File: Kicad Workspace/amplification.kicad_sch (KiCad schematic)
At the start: 1 part, among them U5 TPA3255DDV

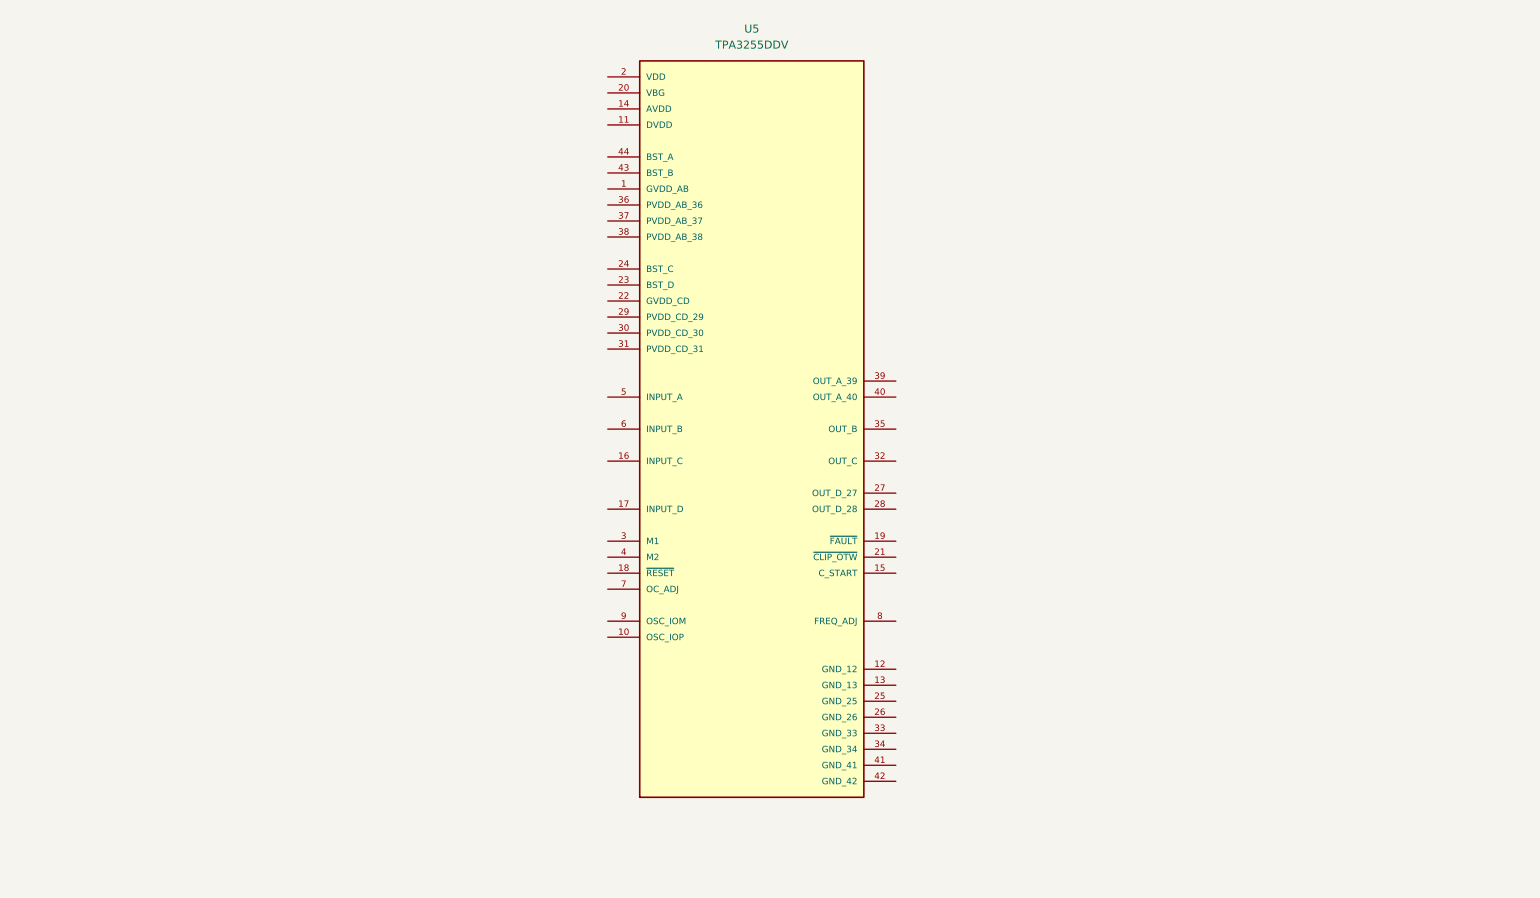
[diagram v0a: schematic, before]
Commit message: feat: ampli stage work in progress
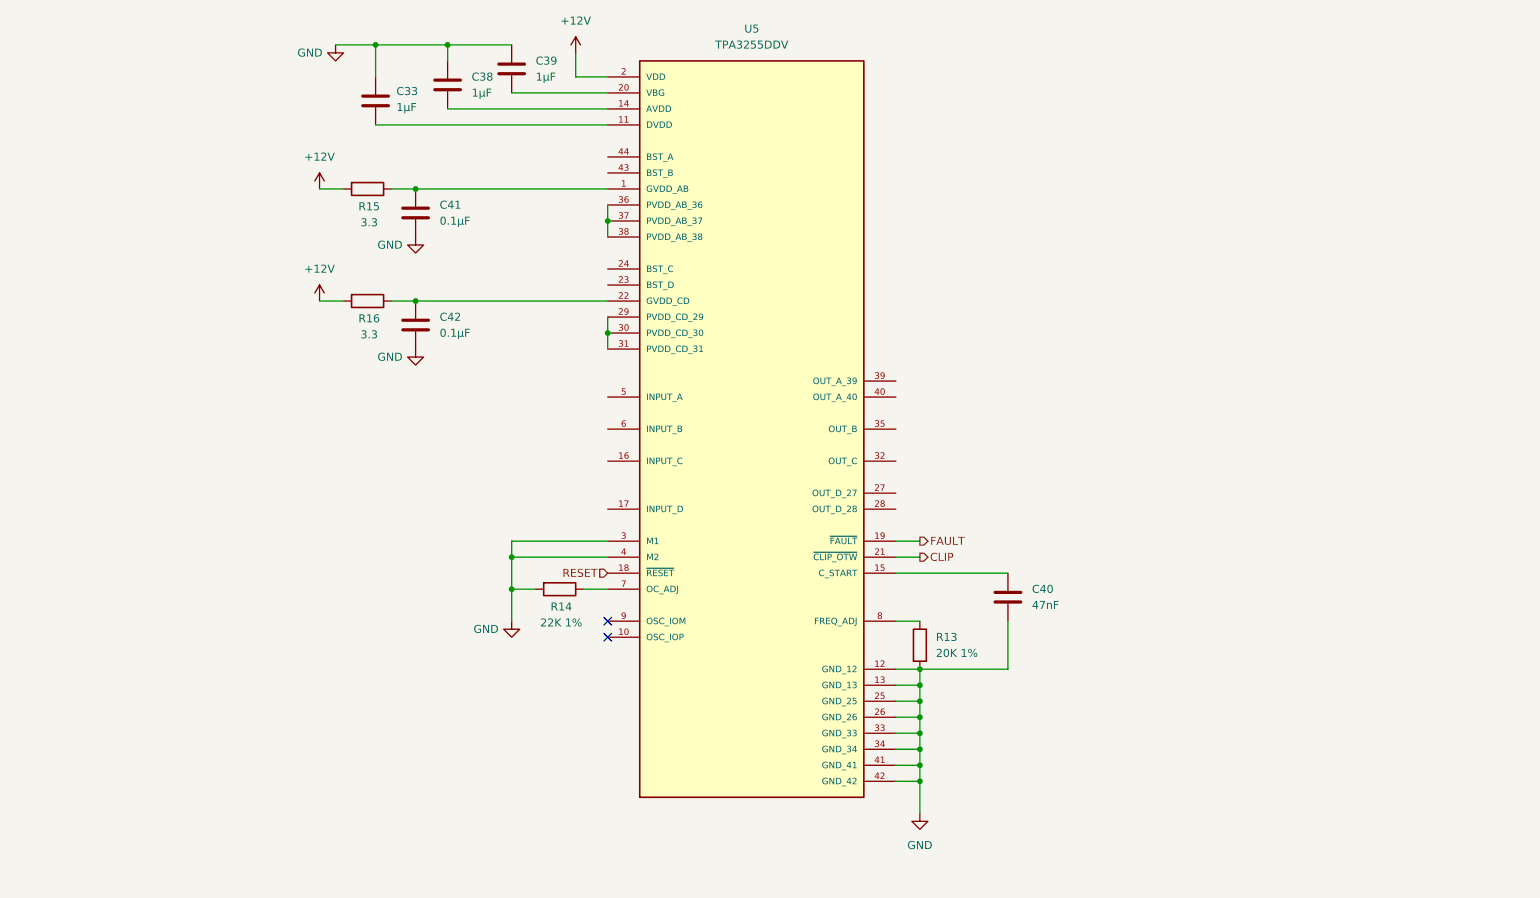
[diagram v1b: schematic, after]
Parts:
- added C33, C38, C39: 1µF, Capacitor_SMD:C_0201_0603Metric, symbol Device:C
- added C40: 47nF, Capacitor_SMD:C_0201_0603Metric, symbol Device:C
- added C41, C42: 0.1µF, Capacitor_SMD:C_01005_0402Metric, symbol Device:C
- added R13: 20K 1%, Resistor_SMD:R_0805_2012Metric, symbol Device:R
- added R14: 22K 1%, Resistor_SMD:R_0805_2012Metric, symbol Device:R
- added R15, R16: 3.3, Resistor_SMD:R_0201_0603Metric, symbol Device:R
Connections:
- net at U5.1 (GVDD_AB): now also C41.2, R15.1
- net at U5.11 (DVDD): now also C33.2
- net GND: now reaches U5.12 (GND_12)
- net GND: now also U5.13 (GND_13), U5.25 (GND_25), U5.26 (GND_26), U5.3 (M1), U5.33 (GND_33), U5.34 (GND_34), U5.4 (M2), U5.41 (GND_41), U5.42 (GND_42), C33.1, C38.2, C39.2, C40.2, C41.1, C42.1, R13.2, R14.2
- net at U5.14 (AVDD): now also C38.1
- net at U5.15 (C_START): now also C40.1
- net RESET: now reaches U5.18 (~{RESET})
- net FAULT: now reaches U5.19 (~{FAULT})
- net +12V: now reaches U5.2 (VDD)
- net +12V: now also R15.2, R16.2
- net at U5.20 (VBG): now also C39.1
- net CLIP: now reaches U5.21 (~{CLIP_OTW})
- net at U5.22 (GVDD_CD): now also C42.2, R16.1
- net at U5.29 (PVDD_CD_29): now also U5.30 (PVDD_CD_30), U5.31 (PVDD_CD_31)
- net at U5.36 (PVDD_AB_36): now also U5.37 (PVDD_AB_37), U5.38 (PVDD_AB_38)
- net at U5.7 (OC_ADJ): now also R14.1
- net at U5.8 (FREQ_ADJ): now also R13.1
- no-connect marks 0 -> 2

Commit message: feat: TPA3255 power 48V + clean output
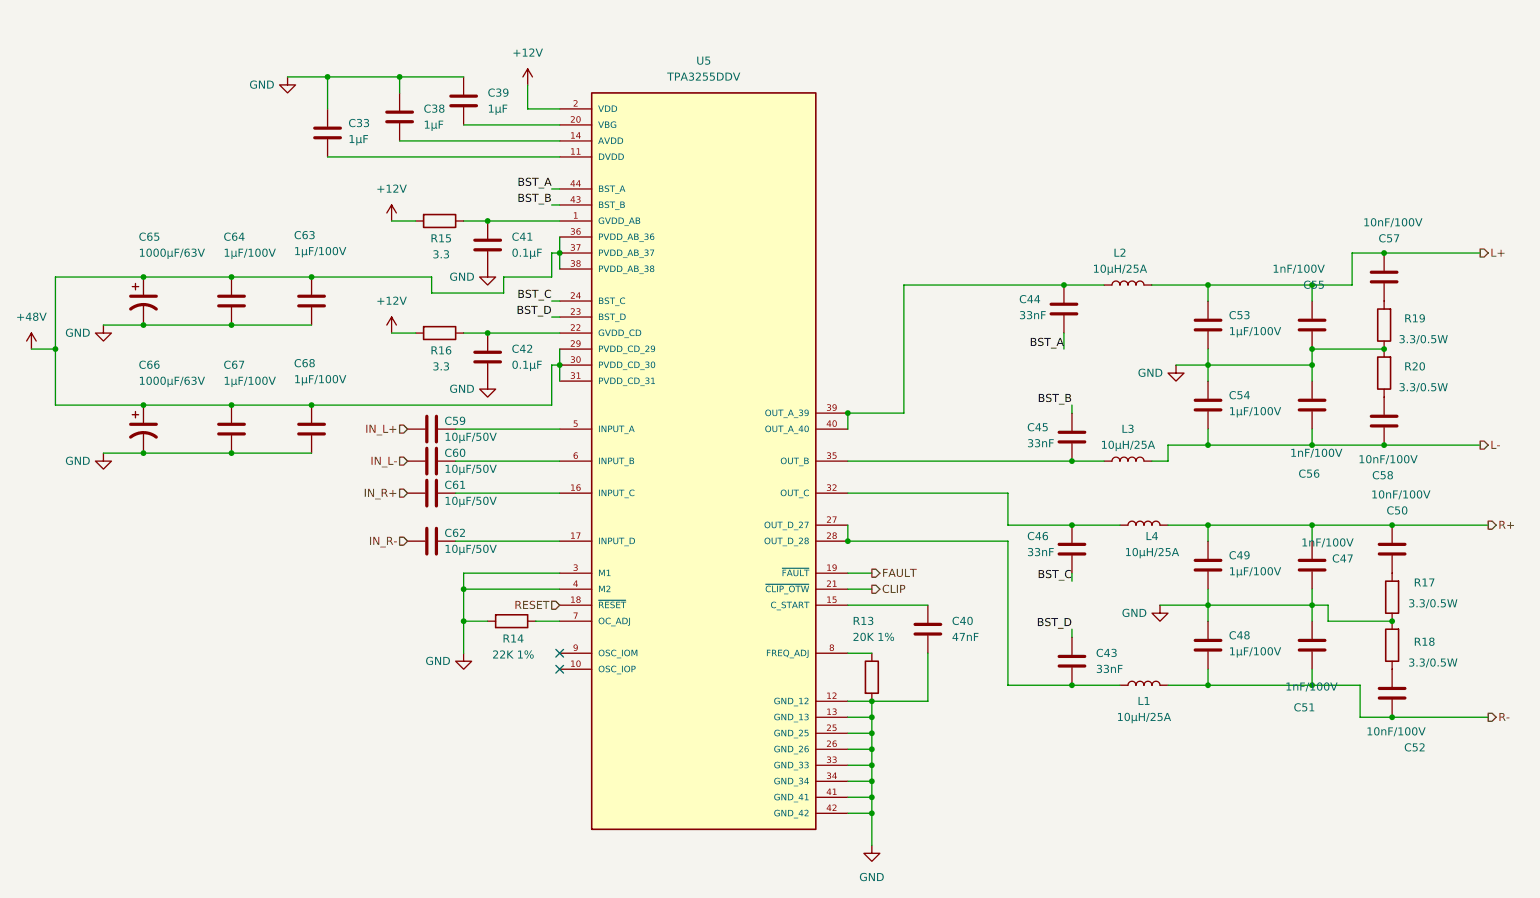
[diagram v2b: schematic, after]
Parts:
- added C43, C44, C45, C46: 33nF, Capacitor_SMD:C_0201_0603Metric, symbol Device:C
- added C47, C51, C55, C56: 1nF/100V, Capacitor_SMD:C_0201_0603Metric, symbol Device:C
- added C48, C49, C53, C54, C63, C64, C67, C68: 1µF/100V, Capacitor_THT:C_Rect_L10.0mm_W4.0mm_P7.50mm_MKS4, symbol Device:C
- added C50, C52, C57, C58: 10nF/100V, Capacitor_SMD:C_0805_2012Metric, symbol Device:C
- added C59, C60, C61, C62: 10µF/50V, Capacitor_THT:C_Radial_D6.3mm_H11.0mm_P2.50mm, symbol Device:C
- added C65, C66: 1000µF/63V, Capacitor_THT:CP_Radial_D16.0mm_P7.50mm, symbol Device:C_Polarized_US
- added L1, L2, L3, L4: 10µH/25A, symbol Device:L
- added R17, R18, R19, R20: 3.3/0.5W, Resistor_SMD:R_1206_3216Metric, symbol Device:R
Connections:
- net GND: now also C47.1, C48.1, C49.2, C51.2, C53.2, C54.1, C55.1, C56.2, C63.2, C64.2, C65.2, C66.2, C67.2, C68.2, R17.1, R18.2, R19.1, R20.2
- net at U5.16 (INPUT_C): now also C61.1
- net at U5.17 (INPUT_D): now also C62.1
- net BST_D: now reaches U5.23 (BST_D)
- net BST_D: now also C43.1
- net BST_C: now reaches U5.24 (BST_C)
- net BST_C: now also C46.2
- net at U5.27 (OUT_D_27): now also U5.28 (OUT_D_28), C43.2, L1.1
- net +48V: now reaches U5.29 (PVDD_CD_29), U5.30 (PVDD_CD_30), U5.31 (PVDD_CD_31)
- net +48V: now also U5.36 (PVDD_AB_36), U5.37 (PVDD_AB_37), U5.38 (PVDD_AB_38), C63.1, C64.1, C65.1, C66.1, C67.1, C68.1
- net at U5.32 (OUT_C): now also C46.1, L4.1
- net at U5.35 (OUT_B): now also C45.2, L3.1
- net at U5.39 (OUT_A_39): now also U5.40 (OUT_A_40), C44.1, L2.1
- net BST_B: now reaches U5.43 (BST_B)
- net BST_B: now also C45.1
- net BST_A: now reaches U5.44 (BST_A)
- net BST_A: now also C44.2
- net at U5.5 (INPUT_A): now also C59.1
- net at U5.6 (INPUT_B): now also C60.1
- new net: C52.2, R18.1
- new net: C50.1, R17.2
- new net: C57.1, R19.2
- new net: C58.2, R20.1
- new net IN_L+: C59.2
- new net IN_L-: C60.2
- new net IN_R+: C61.2
- new net IN_R-: C62.2
- new net L+: C53.1, C55.2, C57.2, L2.2
- new net L-: C54.2, C56.1, C58.1, L3.2
- new net R+: C47.2, C49.1, C50.2, L4.2
- new net R-: C48.2, C51.1, C52.1, L1.2
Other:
- moved on the sheet: C33, C38, C39, C40, C41, C42, R13, R14, R15, R16, U5

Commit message: feat: alim stage done + adapt to 36V input voltage instead of 48
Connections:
- net +48V renamed +36V
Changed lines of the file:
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@@
 		(in_pos_files yes)
 		(dnp no)
-		(fields_autoplaced yes)
 		(property "Reference" "#PWR054"
 			(at 25.4 82.55 0)
@@
 			)
 		)
-		(property "Value" "+48V"
-			(at 25.4 73.66 0)
+		(property "Value" "+36V"
+			(at 23.876 74.168 0)
 			(show_name no)
 			(do_not_autoplace no)
@@
 					(size 1.27 1.27)
 				)
+				(justify left)
 			)
 		)

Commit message: fix: Bus fix with correct syntax
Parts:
- added J5: L+, Connector_Wire:SolderWirePad_1x01_SMD_2x4mm, symbol Connector:Conn_01x01_Pin
- added J6: L-, Connector_Wire:SolderWirePad_1x01_SMD_2x4mm, symbol Connector:Conn_01x01_Pin
- added J7: R+, Connector_Wire:SolderWirePad_1x01_SMD_2x4mm, symbol Connector:Conn_01x01_Pin
- added J8: R-, Connector_Wire:SolderWirePad_1x01_SMD_2x4mm, symbol Connector:Conn_01x01_Pin
- U5: footprint TPA3255DDV:SOP63P810X120-44N -> FootPrints:TPA3255
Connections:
- net L+: no longer names the net of C53.1, C55.2, C57.2, L2.2
- net L+: now also J5.1 (Pin_1)
- net L-: no longer names the net of C54.2, C56.1, C58.1, L3.2
- net L-: now also J6.1 (Pin_1)
- net R+: no longer names the net of C47.2, C49.1, C50.2, L4.2
- net R+: now also J7.1 (Pin_1)
- net R-: no longer names the net of C48.2, C51.1, C52.1, L1.2
- net R-: now also J8.1 (Pin_1)

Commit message: feat: selecting TPA3255 output inductances
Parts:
- L1, L2, L3, L4: footprint (none) -> FootPrints:IND_SER2915L-103KL
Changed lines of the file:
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@@
 			)
 		)
-		(property "Footprint" ""
+		(property "Footprint" "FootPrints:IND_SER2915L-103KL"
 			(at 201.93 132.08 0)
 			(hide yes)
@@
 			)
 		)
-		(property "Footprint" ""
+		(property "Footprint" "FootPrints:IND_SER2915L-103KL"
 			(at 201.93 106.68 0)
 			(hide yes)
@@
 			)
 		)
-		(property "Footprint" ""
+		(property "Footprint" "FootPrints:IND_SER2915L-103KL"
 			(at 199.39 96.52 0)
 			(hide yes)
@@
 			)
 		)
-		(property "Footprint" ""
+		(property "Footprint" "FootPrints:IND_SER2915L-103KL"
 			(at 199.39 68.58 0)
 			(hide yes)
